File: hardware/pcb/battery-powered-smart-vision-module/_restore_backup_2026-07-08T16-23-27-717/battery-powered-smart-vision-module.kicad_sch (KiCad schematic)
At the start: 15 parts, among them J1 Conn_01x02, J3 I2C Header, J4 GPIO Header, SW2 SW_SPST

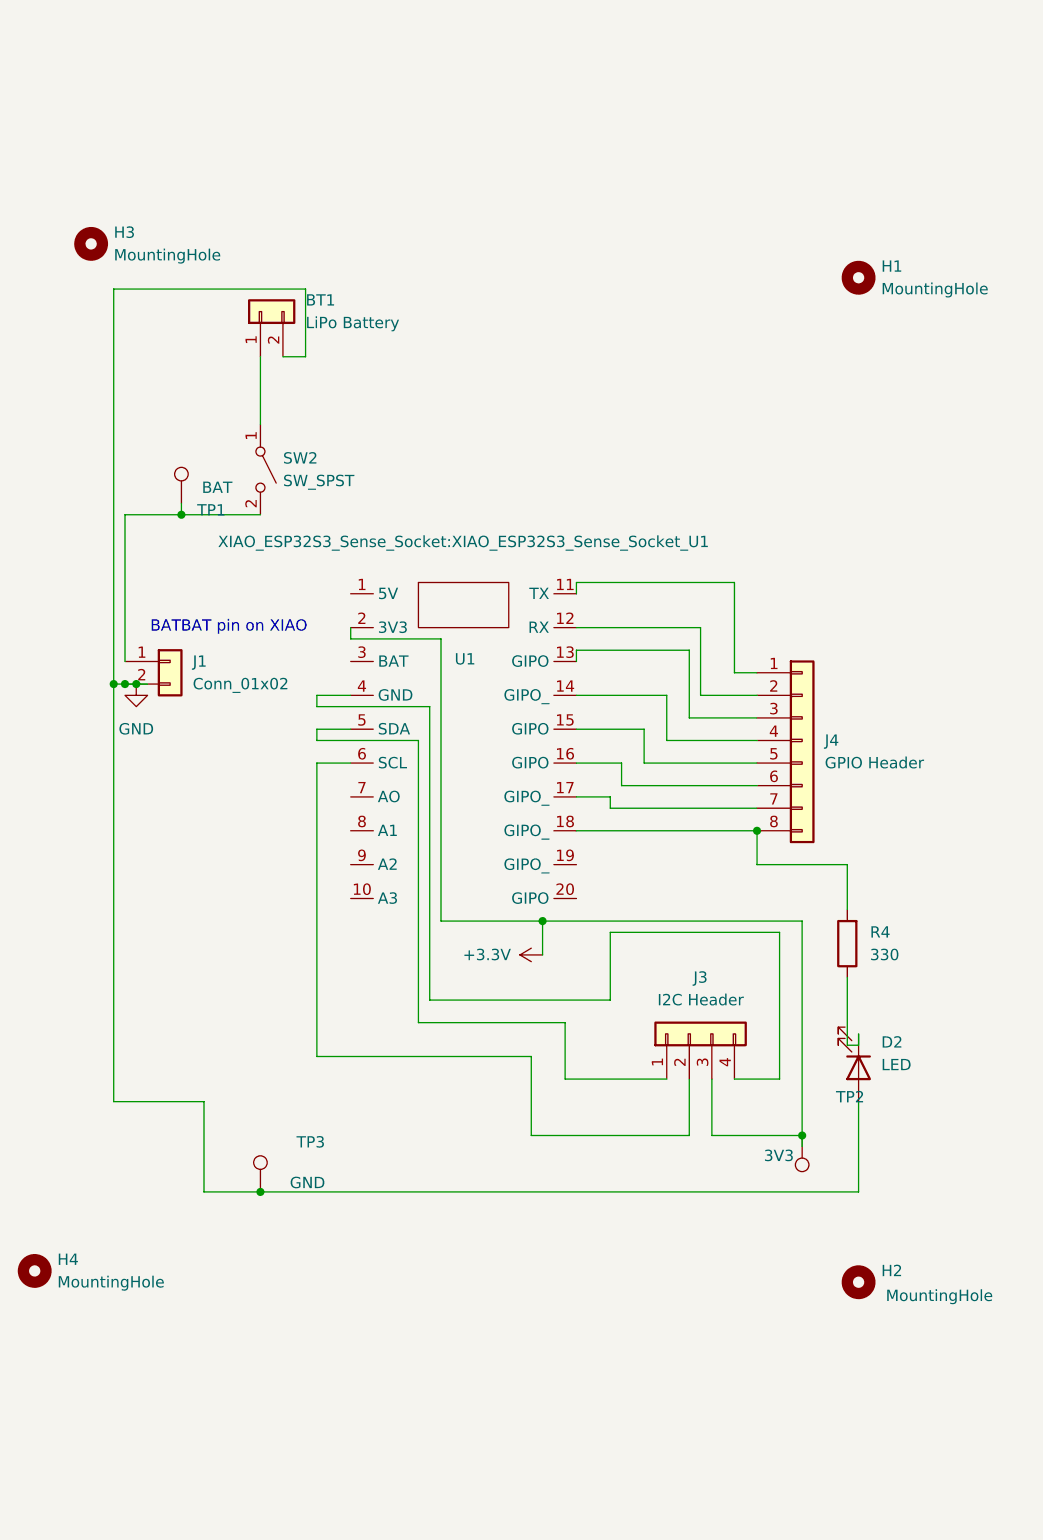
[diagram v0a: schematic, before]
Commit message: Complete PCB design updates and hardware integration
Updated KiCad schematic, PCB layout, custom XIAO ESP32S3 Sense footprint, project files, manufacturing outputs, and hardware documentation. Continued development of the battery-powered smart vision module.
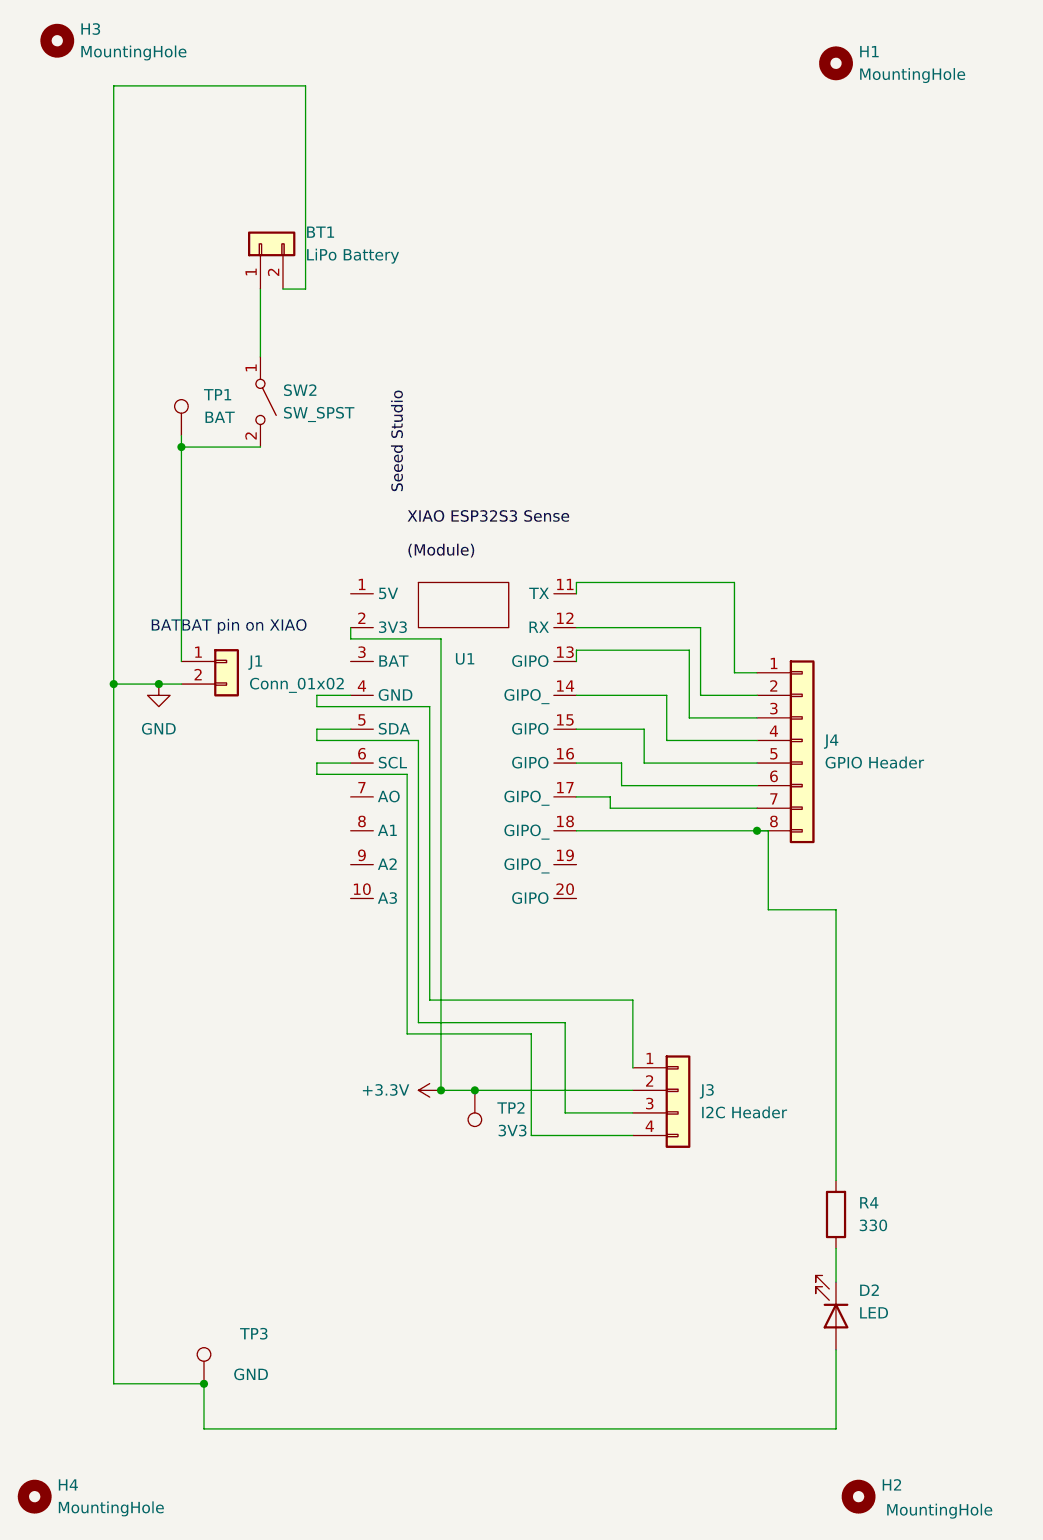
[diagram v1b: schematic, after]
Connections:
- net +3.3V: now also J3.2 (Pin_2); no longer J3.3 (Pin_3)
- net at U1.4 (GND): now also J3.1 (Pin_1); no longer J3.4 (Pin_4)
- net at U1.5 (SDA): now also J3.3 (Pin_3); no longer J3.1 (Pin_1)
- net at U1.6 (SCL): now also J3.4 (Pin_4); no longer J3.2 (Pin_2)
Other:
- moved on the sheet: BT1, D2, H1, H2, H3, H4, J1, J3, R4, SW2, TP1, TP2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
